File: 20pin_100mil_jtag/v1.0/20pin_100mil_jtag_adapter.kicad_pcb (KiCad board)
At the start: 2 copper layers, 14 x 27 mm, 49 parts, among them X1 JTAG-10, X2 JTAG-20

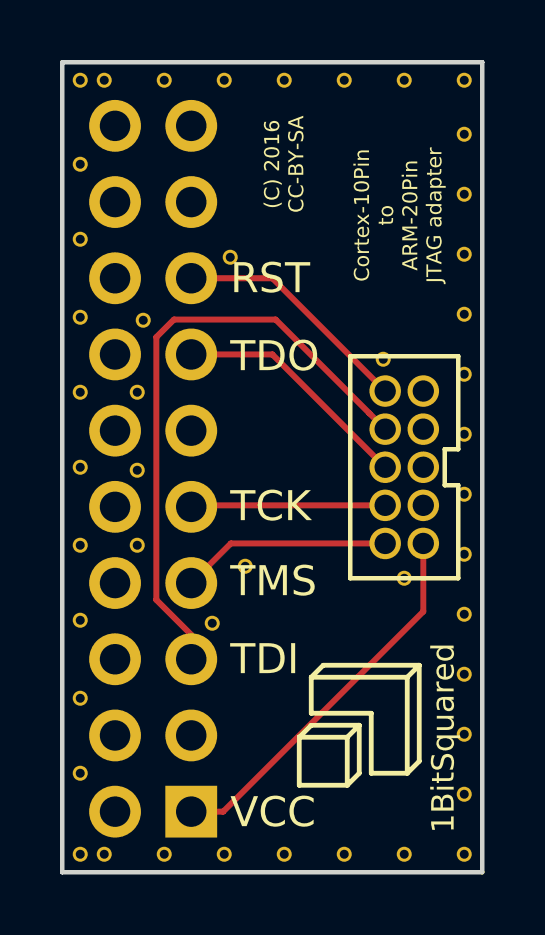
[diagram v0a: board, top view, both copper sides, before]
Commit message: Made the adapter name bit more explicit, and minor cleanups.
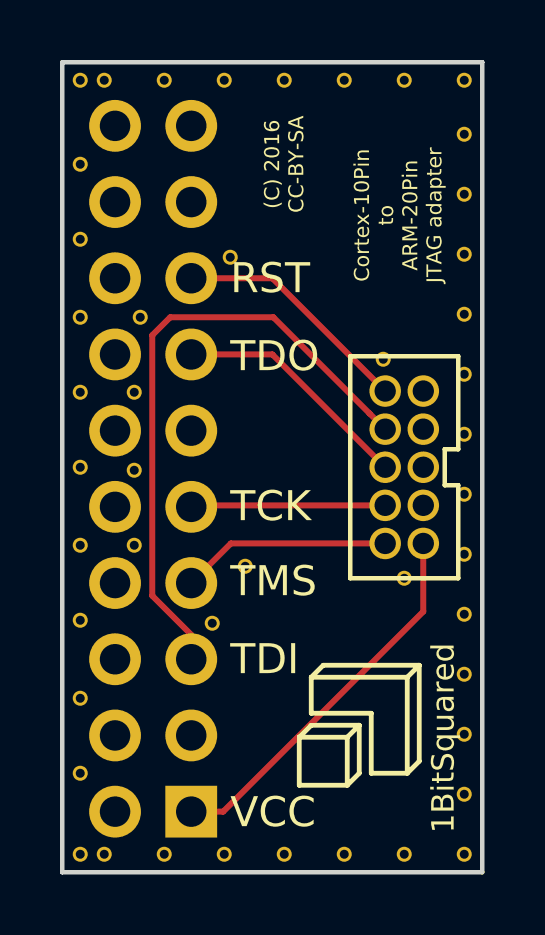
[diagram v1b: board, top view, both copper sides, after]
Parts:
- moved REF** 0.14 mm to (22.6, 28.5)
- moved REF** 0.10 mm to (22.4, 31.0)
- moved REF** 0.10 mm to (22.4, 33.6)
- moved REF** 0.10 mm to (22.4, 36.1)
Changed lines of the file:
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@@
     (links 63)
     (no_connects 0)
-    (area 19.774999 19.913475 34.075001 50.351191)
+    (area 19.924999 19.924999 34.075001 47.075001)
     (thickness 1.6)
     (drawings 19)
@@
   )
   (module pkl_misc:via0305 (layer F.Cu)
-    (at 22.7 28.6)
-    (fp_text reference REF** (at 0 0.35) (layer F.SilkS) hide
-      (effects (font (size 0.127 0.127) (thickness 0.03175)))
-    )
-    (fp_text value via0305 (at 0 -0.35) (layer F.Fab) hide
-      (effects (font (size 0.127 0.127) (thickness 0.03175)))
-    )
-    (pad "" thru_hole circle (at 0 0) (size 0.5 0.5) (drill 0.3) (layers *.Cu)
-      (net 1 GND) (zone_connect 2))
-  )
-  (module pkl_misc:via0305 (layer F.Cu)
-    (at 22.5 31)
-    (fp_text reference REF** (at 0 0.35) (layer F.SilkS) hide
-      (effects (font (size 0.127 0.127) (thickness 0.03175)))
-    )
-    (fp_text value via0305 (at 0 -0.35) (layer F.Fab) hide
-      (effects (font (size 0.127 0.127) (thickness 0.03175)))
-    )
-    (pad "" thru_hole circle (at 0 0) (size 0.5 0.5) (drill 0.3) (layers *.Cu)
-      (net 1 GND) (zone_connect 2))
-  )
-  (module pkl_misc:via0305 (layer F.Cu)
-    (at 22.5 33.6)
-    (fp_text reference REF** (at 0 0.35) (layer F.SilkS) hide
-      (effects (font (size 0.127 0.127) (thickness 0.03175)))
-    )
-    (fp_text value via0305 (at 0 -0.35) (layer F.Fab) hide
-      (effects (font (size 0.127 0.127) (thickness 0.03175)))
-    )
-    (pad "" thru_hole circle (at 0 0) (size 0.5 0.5) (drill 0.3) (layers *.Cu)
-      (net 1 GND) (zone_connect 2))
-  )
-  (module pkl_misc:via0305 (layer F.Cu)
-    (at 22.5 36.1)
+    (at 22.6 28.5)
+    (fp_text reference REF** (at 0 0.35) (layer F.SilkS) hide
+      (effects (font (size 0.127 0.127) (thickness 0.03175)))
+    )
+    (fp_text value via0305 (at 0 -0.35) (layer F.Fab) hide
+      (effects (font (size 0.127 0.127) (thickness 0.03175)))
+    )
+    (pad "" thru_hole circle (at 0 0) (size 0.5 0.5) (drill 0.3) (layers *.Cu)
+      (net 1 GND) (zone_connect 2))
+  )
+  (module pkl_misc:via0305 (layer F.Cu)
+    (at 22.4 31)
+    (fp_text reference REF** (at 0 0.35) (layer F.SilkS) hide
+      (effects (font (size 0.127 0.127) (thickness 0.03175)))
+    )
+    (fp_text value via0305 (at 0 -0.35) (layer F.Fab) hide
+      (effects (font (size 0.127 0.127) (thickness 0.03175)))
+    )
+    (pad "" thru_hole circle (at 0 0) (size 0.5 0.5) (drill 0.3) (layers *.Cu)
+      (net 1 GND) (zone_connect 2))
+  )
+  (module pkl_misc:via0305 (layer F.Cu)
+    (at 22.4 33.6)
+    (fp_text reference REF** (at 0 0.35) (layer F.SilkS) hide
+      (effects (font (size 0.127 0.127) (thickness 0.03175)))
+    )
+    (fp_text value via0305 (at 0 -0.35) (layer F.Fab) hide
+      (effects (font (size 0.127 0.127) (thickness 0.03175)))
+    )
+    (pad "" thru_hole circle (at 0 0) (size 0.5 0.5) (drill 0.3) (layers *.Cu)
+      (net 1 GND) (zone_connect 2))
+  )
+  (module pkl_misc:via0305 (layer F.Cu)
+    (at 22.4 36.1)
     (fp_text reference REF** (at 0 0.35) (layer F.SilkS) hide
       (effects (font (size 0.127 0.127) (thickness 0.03175)))
@@
     (pad 9 thru_hole circle (at 2.54 0.635 90) (size 1.05 1.05) (drill 0.71) (layers *.Cu *.Mask F.SilkS)
       (net 1 GND))
+    (model Pin_Headers.3dshapes/Pin_Header_Straight_2x05.wrl
+      (at (xyz 0 0 0))
+      (scale (xyz 0.5 0.5 0.5))
+      (rotate (xyz 0 0 0))
+    )
   )
   (module pkl_misc:via0305 (layer F.Cu)
@@
   (segment (start 27.005 29.74) (end 24.3 29.74) (width 0.2) (layer F.Cu) (net 11))
   (segment (start 24.3 39.9) (end 24.3 39.08213) (width 0.2) (layer F.Cu) (net 12))
-  (segment (start 24.3 39.08213) (end 23.136399 37.918529) (width 0.2) (layer F.Cu) (net 12))
-  (segment (start 23.136399 37.918529) (end 23.136399 29.163601) (width 0.2) (layer F.Cu) (net 12))
-  (segment (start 23.136399 29.163601) (end 23.723601 28.576399) (width 0.2) (layer F.Cu) (net 12))
-  (segment (start 23.723601 28.576399) (end 27.111399 28.576399) (width 0.2) (layer F.Cu) (net 12))
+  (segment (start 24.3 39.08213) (end 23 37.78213) (width 0.2) (layer F.Cu) (net 12))
+  (segment (start 23 37.78213) (end 23 29.1) (width 0.2) (layer F.Cu) (net 12))
+  (segment (start 23 29.1) (end 23.6 28.5) (width 0.2) (layer F.Cu) (net 12))
+  (segment (start 27.035 28.5) (end 30.240001 31.705001) (width 0.2) (layer F.Cu) (net 12))
+  (segment (start 23.6 28.5) (end 27.035 28.5) (width 0.2) (layer F.Cu) (net 12))
   (segment (start 30.240001 31.705001) (end 30.765 32.23) (width 0.2) (layer F.Cu) (net 12))
-  (segment (start 27.111399 28.576399) (end 30.240001 31.705001) (width 0.2) (layer F.Cu) (net 12))
   (segment (start 30.765 30.96) (end 27.005 27.2) (width 0.2) (layer F.Cu) (net 13))
   (segment (start 27.005 27.2) (end 24.3 27.2) (width 0.2) (layer F.Cu) (net 13))

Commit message: Added VCC jumper to the adapter.
The VCC jumper is connected by default, but it makes it possible to cut
the circuit open and then use a solder jumper to close it again. Some
added flexibility... :)
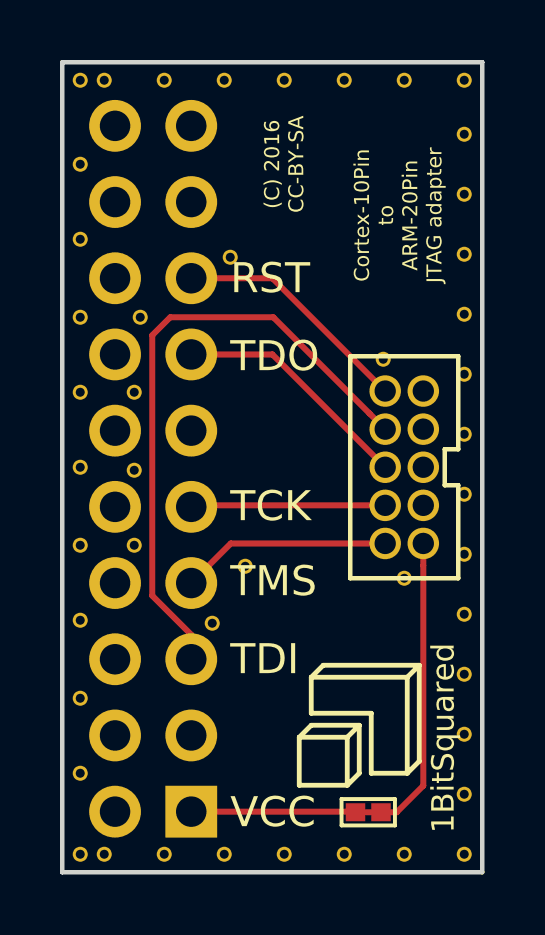
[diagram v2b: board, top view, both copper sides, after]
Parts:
- added J1: Jumper, pkl_jumpers:J_0402, F.Cu at (30.2, 45.0)
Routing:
- net /VCC: track 12.8 -> 16.2 mm
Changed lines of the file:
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@@
-(kicad_pcb (version 4) (host pcbnew 4.0.1-3.201512221402+6198~38~ubuntu14.04.1-stable)
+(kicad_pcb (version 4) (host pcbnew 4.0.1-4.201602132031+6195~38~ubuntu14.04.1-stable)
   (general
-    (links 63)
-    (no_connects 0)
+    (links 65)
+    (no_connects 2)
     (area 19.924999 19.924999 34.075001 47.075001)
     (thickness 1.6)
     (drawings 19)
-    (tracks 18)
+    (tracks 22)
     (zones 0)
-    (modules 49)
+    (modules 50)
     (nets 14)
   )
@@
     (47 F.CrtYd user)
     (48 B.Fab user)
-    (49 F.Fab user)
+    (49 F.Fab user hide)
   )
   (setup
@@
     (descr "Through hole socket strip")
     (tags "socket strip")
-    (fp_text reference X2 (at 11.8 5 90) (layer B.Fab)
+    (fp_text reference X2 (at 11.38 -7 90) (layer B.Fab)
       (effects (font (size 1 1) (thickness 0.15)) (justify mirror))
     )
-    (fp_text value JTAG-20 (at 11.58 2.8 90) (layer B.Fab)
+    (fp_text value JTAG-20 (at 11.48 -5.2 90) (layer B.Fab)
       (effects (font (size 1 1) (thickness 0.15)) (justify mirror))
     )
@@
     (fp_line (start -0.4 -0.4) (end -0.4 -2) (layer F.SilkS) (width 0.16))
   )
+  (module pkl_jumpers:J_0402 (layer F.Cu)
+    (at 30.2 45 180)
+    (descr "Jumper SMD 0402, reflow soldering")
+    (tags "jumper 0402")
+    (solder_mask_margin 0.075)
+    (attr smd)
+    (fp_text reference J1 (at 0 -1.1 180) (layer F.Fab)
+      (effects (font (size 0.635 0.635) (thickness 0.1)))
+    )
+    (fp_text value Jumper (at 0 1.2 180) (layer F.Fab)
+      (effects (font (size 0.635 0.635) (thickness 0.1)))
+    )
+    (fp_line (start -0.89 -0.44) (end -0.89 0.44) (layer F.SilkS) (width 0.13))
+    (fp_line (start 0.89 -0.44) (end 0.89 0.44) (layer F.SilkS) (width 0.13))
+    (fp_line (start -0.95 -0.5) (end 0.95 -0.5) (layer F.CrtYd) (width 0.05))
+    (fp_line (start -0.95 0.5) (end 0.95 0.5) (layer F.CrtYd) (width 0.05))
+    (fp_line (start -0.95 -0.5) (end -0.95 0.5) (layer F.CrtYd) (width 0.05))
+    (fp_line (start 0.95 -0.5) (end 0.95 0.5) (layer F.CrtYd) (width 0.05))
+    (fp_line (start -0.89 -0.44) (end 0.89 -0.44) (layer F.SilkS) (width 0.13))
+    (fp_line (start 0.89 0.44) (end -0.89 0.44) (layer F.SilkS) (width 0.13))
+    (pad 1 smd rect (at -0.425 0 180) (size 0.65 0.6) (layers F.Cu F.Paste F.Mask)
+      (net 9 /VCC))
+    (pad 2 smd rect (at 0.425 0 180) (size 0.65 0.6) (layers F.Cu F.Paste F.Mask)
+      (net 9 /VCC))
+  )
   (gr_text "(C) 2016\nCC-BY-SA" (at 27.4 23.4 90) (layer F.SilkS)
     (effects (font (size 0.5 0.5) (thickness 0.125)))
@@
   (segment (start 30.765 36.04) (end 25.62 36.04) (width 0.2) (layer F.Cu) (net 8))
   (segment (start 25.62 36.04) (end 24.3 37.36) (width 0.2) (layer F.Cu) (net 8))
-  (segment (start 32.035 36.04) (end 32.035 38.3086) (width 0.2) (layer F.Cu) (net 9))
-  (segment (start 32.035 38.3086) (end 25.3636 44.98) (width 0.2) (layer F.Cu) (net 9))
-  (segment (start 25.3636 44.98) (end 24.3 44.98) (width 0.2) (layer F.Cu) (net 9))
+  (segment (start 30.625 45) (end 31.15 45) (width 0.2) (layer F.Cu) (net 9))
+  (segment (start 31.15 45) (end 32.035 44.115) (width 0.2) (layer F.Cu) (net 9))
+  (segment (start 32.035 44.115) (end 32.035 36.782462) (width 0.2) (layer F.Cu) (net 9))
+  (segment (start 32.035 36.782462) (end 32.035 36.04) (width 0.2) (layer F.Cu) (net 9))
+  (segment (start 29.775 45) (end 30.625 45) (width 0.2) (layer F.Cu) (net 9))
+  (segment (start 24.3 44.98) (end 29.755 44.98) (width 0.2) (layer F.Cu) (net 9))
+  (segment (start 29.755 44.98) (end 29.775 45) (width 0.2) (layer F.Cu) (net 9))
   (segment (start 30.765 34.77) (end 24.35 34.77) (width 0.2) (layer F.Cu) (net 10))
   (segment (start 24.35 34.77) (end 24.3 34.82) (width 0.2) (layer F.Cu) (net 10))
